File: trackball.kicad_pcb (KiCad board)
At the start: 6 copper layers, 65 x 85 mm, 241 parts, among them J2 ZX-PM2.0-2-4PY, Q1 XR2302, Q2 XR2302, SW1 HX TC-5608-Y, SW2 HX TC-5608-Y, SW3 HX TC-5608-Y, SW4 HX TC-5608-Y, SW5 HX TC-5608-Y, SW6 HX TC-5608-Y, SW7 HX TC-5608-Y, SW8 HX TC-5608-Y, SW9 TS-1010-C-A, U1 USB-TYPE-C-017, U10 WS2812B, U11 WS2812B, U12 WS2812B, U13 WS2812B, U14 WS2812B, U15 WS2812B, U16 WS2812B, U17 WS2812B, U18 WS2812B, U19 WS2812B, U2 SY80004DQD, U20 WS2812B, U21 WS2812B, U3 SY80004DQD, U4 PMW3610, U5 PMW3610, U6 WS2812B, U7 WS2812B, U8 WS2812B, U9 WS2812B, X1 XL7EL89CKI-111YLC-32M

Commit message: feat: 1k dongle, rev5 hw (wip)
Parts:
- removed C16, C31: 0201B103K160NT, easyeda2kicad:C0201
- removed R35: RC-01W103JT, easyeda2kicad:R0201
- removed R36: 0201WMF1603TEE, easyeda2kicad:R0201
- removed U_RE1, U_RE2: GT-EVA01AA-L1, easyeda2kicad:RES-ADJ-SMD_GT-EVA01AA-L1
- added C61: GRM155R60J226ME11D, easyeda2kicad:C0402, F.Cu at (39.9, 40.6)
- added C64: GRM155R60J226ME11D, easyeda2kicad:C0402, F.Cu at (47.5, 47.2)
- added ENC1: EC05E1220401, easyeda2kicad:SW-SMD_EC05E1220401, F.Cu at (67.5, 67.1)
- added ENC2: EC05E1220401, easyeda2kicad:SW-SMD_EC05E1220401, F.Cu at (67.5, 78.1)
- added Q3: AO3415A_C5350990, easyeda2kicad:SOT-23-3_L2.9-W1.6-P1.90-LS2.8-BR, F.Cu at (42.7, 42.2)
- added Q4: XR2302, easyeda2kicad:SOT-23-3_L2.9-W1.3-P0.95-LS2.4-BR, F.Cu at (46.1, 42.4)
- added R23: 0201WMF1603TEE, easyeda2kicad:R0201, F.Cu at (48.7, 44.9)
- added R49: RC-01W103JT, easyeda2kicad:R0201, F.Cu at (48.4, 43.9)
- added R6: RC-01W103JT, easyeda2kicad:R0201, F.Cu at (76.6, 47.7)
- added R7: RC-01W103JT, easyeda2kicad:R0201, F.Cu at (43.8, 44.1)
- added R8: RC-01W103JT, easyeda2kicad:R0201, F.Cu at (44.9, 40.7)
- added U22: TPS2116DRLR, easyeda2kicad:SOT-583-8_L2.1-W1.6-P0.50-LS1.6-BL, F.Cu at (45.6, 45.6)
- C30: value 0201B103K160NT -> 0201B821K500NT
- J2: value ZX-PM2.0-2-4PY -> AFH34-S08FIA-1H; footprint easyeda2kicad:HDR-TH_8P-P2.00-V-F-R2-C4-S2.00 -> easyeda2kicad:FPC-SMD_8P-P0.50_JS_AFH34-S08FIA-1H
- R12, R13, R14, R21: value RC-01W103JT -> RC0201JR-075K1L
- R18: value RT0402BRE0750RL -> RC-01W103JT; footprint easyeda2kicad:R0402 -> easyeda2kicad:R0201
- R22: value 0201WMF1603TEE -> RC0201JR-075K1L
- R3, R50, R51: value ~ -> (none)
- SW9: value TS-1010-C-A -> (none)
- moved R22 39.8 mm to (58.3, 43.7)
- moved R21 37.3 mm to (71.2, 45.3), turned to -90 degrees
- moved R32 10.4 mm to (38.7, 66.4)
- moved Q2 8.53 mm to (51.4, 45.3)
- moved R27 5.13 mm to (71.2, 117.1)
- moved R31 4.93 mm to (36.9, 93.9), turned to 90 degrees
- moved C66 2.78 mm to (50.0, 40.7), turned to -90 degrees
- moved R18 2.75 mm to (47.4, 45.2), turned to -90 degrees
- moved C32 2.02 mm to (71.5, 118.0), turned to 180 degrees
- moved R9 1.98 mm to (48.4, 40.9), turned to 0 degrees
- moved R34 1.44 mm to (70.8, 119.1), turned to 0 degrees
- moved J2 1.43 mm to (91.0, 115.1), turned to -135 degrees
- moved R28 1.17 mm to (89.5, 60.2)
- moved R12 1.09 mm to (41.0, 46.6), turned to 90 degrees
- moved R13 1.09 mm to (42.0, 46.2), turned to -90 degrees
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- renumbered ENC.ANY to ENC.ANY.1, ENC.ANY to ENC.ANY.2, SENS.ANY to SENS.ANY.1, SENS.ANY to SENS.ANY.2
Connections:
- C10 pad 1: BAT_VCC -> Net-(Q3-D)
- C15 pad 1: VSYS -> VLOAD
- C18 pad 1: VSYS -> VLOAD
- C3 pad 1: VSYS -> VLOAD
- C5 pad 1: VSYS -> VLOAD
- C7 pad 1: BAT_VCC -> Net-(Q3-D)
- D2 pad 1: SW2 -> SW2_WK
- D2 pad 2: SW1 -> SW1_WK
- D3 pad 1: SW4 -> SW4_WK
- D3 pad 2: SW3 -> SW3_WK
- D4 pad 1: SW6 -> SW6_WK
- D4 pad 2: SW5 -> SW5_WK
- D5 pad 1: SW8 -> SW8_WK
- D5 pad 2: SW7 -> SW7_WK
- ENC.ANY.1 pad 1: D_RE2_1V8 -> D_RE1_1V8
- ENC.ANY.1 pad 2: D_RE2_SW -> D_RE1_GND
- ENC.ANY.1 pad 3: D_RE2_A -> D_RE1_A
- ENC.ANY.1 pad 4: D_RE2_GND -> D_RE1_GND
- ENC.ANY.1 pad 5: D_RE2_B -> D_RE1_B
- ENC.ANY.1 pad 6: D_RE2_GND -> D_RE1_GND
- ENC.ANY.1 pad 7: D_RE2_GND -> D_RE1_GND
- ENC.ANY.1 pad 8: D_RE2_GND -> D_RE1_GND
- ENC.ANY.2 pad 1: D_RE1_1V8 -> D_RE2_1V8
- ENC.ANY.2 pad 2: D_RE1_SW -> D_RE2_GND
- ENC.ANY.2 pad 3: D_RE1_A -> D_RE2_A
- ENC.ANY.2 pad 4: D_RE1_GND -> D_RE2_GND
- ENC.ANY.2 pad 5: D_RE1_B -> D_RE2_B
- ENC.ANY.2 pad 6: D_RE1_GND -> D_RE2_GND
- ENC.ANY.2 pad 7: D_RE1_GND -> D_RE2_GND
- ENC.ANY.2 pad 8: D_RE1_GND -> D_RE2_GND
- ENC.L pad 7: RE1_SW -> GND
- ENC.R pad 7: RE2_SW -> GND
- J2 pad 1: MCU_SWDCLK -> GND
- J2 pad 2: 1V8 -> MCU_SWDCLK
- J2 pad 3: 3V3_EN -> 1V8
- J2 pad 4: 3V3 -> MCU_SWDIO
- J2 pad 5: MCU_SWDIO -> GND
- J2 pad 6: MCU_RESET -> GND
- J2 pad 7: GND -> 1V8
- J2 pad 8: USB_VBUS -> MCU_RESET
- R12 pad 1: 1V8 -> CHG_SDA
- R12 pad 2: CHG_SCL -> 1V8
- R13 pad 1: CHG_SDA -> 1V8
- R13 pad 2: 1V8 -> CHG_SCL
- R14 pad 1: CHG_IRQ -> 1V8
- R14 pad 2: 1V8 -> CHG_IRQ
- R15 pad 2: VSYS -> VLOAD
- R16 pad 1: Net-(R16-Pad1) -> SW8_WK
- R17 pad 1: Net-(R17-Pad1) -> SW7_WK
- R18 pad 1: GND -> Net-(U22-PR1)
- R18 pad 2: MCU_VIB_EN -> USB_VBUS
- R19 pad 1: Net-(R19-Pad1) -> SW1_WK
- R20 pad 1: Net-(R20-Pad1) -> SW2_WK
- R21 pad 1: D_RE1_SW -> Net-(U1-CC1)
- R21 pad 2: Net-(R21-Pad2) -> GND
- R22 pad 1: D_RE1_1V8 -> Net-(U1-CC2)
- R22 pad 2: Net-(R21-Pad2) -> GND
- R26 pad 1: Net-(R26-Pad1) -> SW5_WK
- R27 pad 1: Net-(R27-Pad1) -> SW6_WK
- R29 pad 1: Net-(R29-Pad1) -> SW4_WK
- R30 pad 1: Net-(R30-Pad1) -> SW3_WK
- R31 pad 1: Net-(R29-Pad1) -> SW4_WK
- R32 pad 1: Net-(R30-Pad1) -> SW3_WK
- R33 pad 1: Net-(R26-Pad1) -> SW5_WK
- R34 pad 1: Net-(R27-Pad1) -> SW6_WK
- R37 pad 1: Net-(R19-Pad1) -> SW1_WK
- R38 pad 1: Net-(R20-Pad1) -> SW2_WK
- R39 pad 1: Net-(R16-Pad1) -> SW8_WK
- R4 pad 1: BAT_VCC -> Net-(Q3-D)
- R40 pad 1: Net-(R17-Pad1) -> SW7_WK
- R54 pad 2: VSYS -> VLOAD
- R65 pad 2: VSYS -> VLOAD
- SENS.L pad 9: unconnected-(SENS.L1-Pad9) -> USB_VBUS
- SW1 pad 1: Net-(R19-Pad1) -> SW1_WK
- SW2 pad 1: Net-(R20-Pad1) -> SW2_WK
- SW3 pad 1: Net-(R30-Pad1) -> SW3_WK
- SW4 pad 1: Net-(R29-Pad1) -> SW4_WK
- SW5 pad 1: Net-(R26-Pad1) -> SW5_WK
- SW6 pad 1: Net-(R27-Pad1) -> SW6_WK
- SW7 pad 1: Net-(R17-Pad1) -> SW7_WK
- SW8 pad 1: Net-(R16-Pad1) -> SW8_WK
- SW9 pad 3: unconnected-(SW9-Pad3) -> GND
- SW9 pad 4: unconnected-(SW9-Pad4) -> GND
- U1 pad A5: USB_CC1 -> Net-(U1-CC1)
- U1 pad B5: USB_CC2 -> Net-(U1-CC2)
- U2 pad 6: VSYS -> VLOAD
- U3 pad 6: VSYS -> VLOAD
- U_CHG1 pad 26: USB_CC1 -> unconnected-(U_CHG1-CC1-Pad26)
- U_CHG1 pad 27: USB_CC2 -> unconnected-(U_CHG1-CC2-Pad27)
- U_CHG1 pad 7: BAT_VCC -> Net-(Q3-D)
- U_MCU1 pad AD10: RE1_SW -> ARB2
- U_MCU1 pad T2: RE2_SW -> ARB1
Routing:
- net VLOAD: track 0.00 -> 96.0 mm, vias 0 -> 5
- net VSYS: track 97.6 -> 13.7 mm, vias 5 -> 0
- net 3V3_EN: track 179.6 -> 118.2 mm
- net USB_VBUS: track 183.7 -> 137.5 mm
- net 3V3: track 242.0 -> 203.8 mm, vias 16 -> 14
- net 1V8: track 308.7 -> 270.6 mm, vias 30 -> 28
- net RE1_SW: track 37.6 -> 0.00 mm, vias 2 -> 0
- net RE2_SW: track 35.3 -> 0.00 mm, vias 2 -> 0
- net Net-(Q3-D): track 0.00 -> 33.3 mm, vias 0 -> 4
- net USB_CC1: track 25.7 -> 0.00 mm, vias 2 -> 0
- net SW1_WK: track 0.00 -> 24.2 mm
- net USB_CC2: track 24.2 -> 0.00 mm
- net SW7_WK: track 0.00 -> 22.7 mm, vias 0 -> 2
- net SW4_WK: track 0.00 -> 20.9 mm
- net D_RE2_GND: track 7.84 -> 28.5 mm, vias 5 -> 3
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- added copper zone on B.Cu, net D_RE1_GND
- added copper zone on F.Cu, net D_RE1_GND
- added copper zone on In2.Cu, net D_RE1_GND
- added copper zone on In3.Cu, net D_RE1_GND
- added copper zone on B.Cu, net D_RE2_GND
- added copper zone on F.Cu, net D_RE2_GND
- added copper zone on In2.Cu, net D_RE2_GND
- added copper zone on In3.Cu, net D_RE2_GND
- removed copper zone on In2.Cu, net D_RE1_1V8
- removed copper zone on In3.Cu, net D_RE1_1V8
- removed copper zone on In2.Cu, net D_RE2_1V8
- removed copper zone on In3.Cu, net D_RE2_1V8
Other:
- board text added: "21/01/26"
- board text added: "Jan 2026"
- board text added: "RST"
- board text added: "rev. 05"
- board text removed: "16/10/25"
- board text removed: "Oct 2025"
- board text removed: "rev. 04"

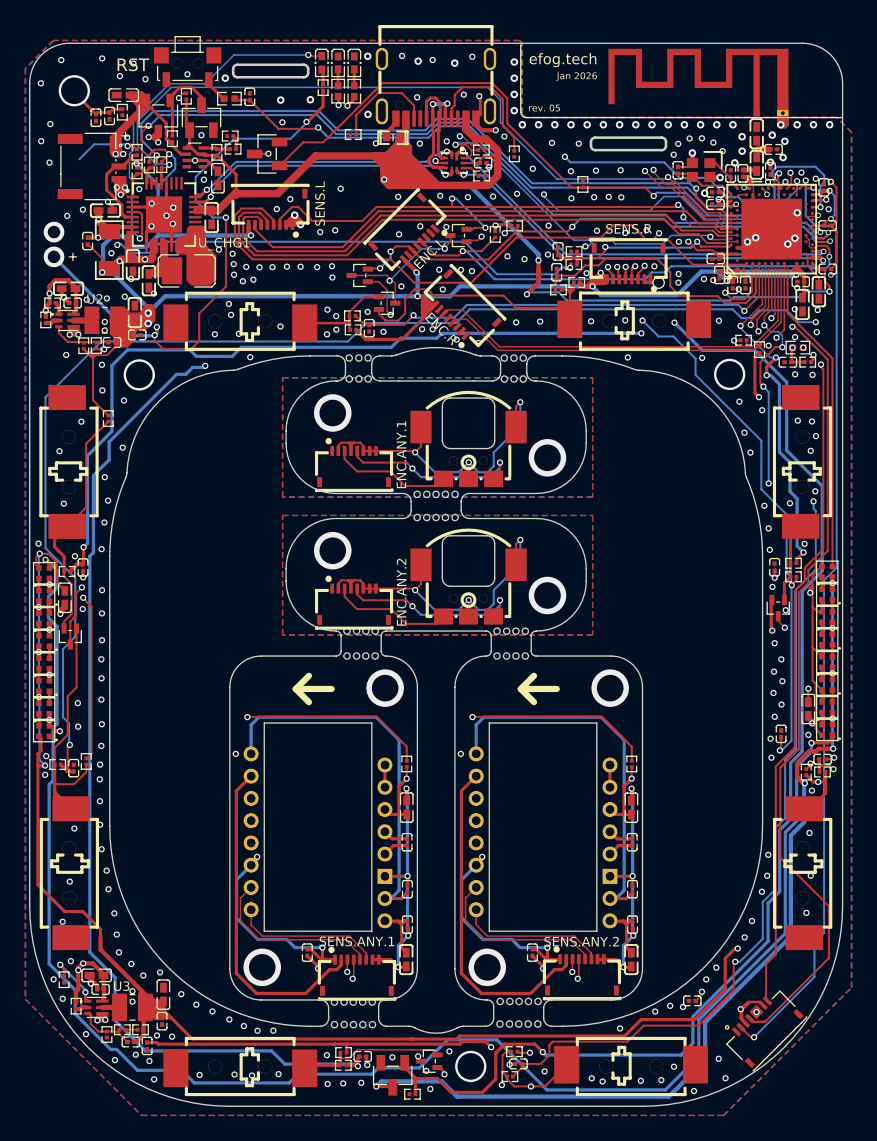
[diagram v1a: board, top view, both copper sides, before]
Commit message: chore: rev5 hw fixes
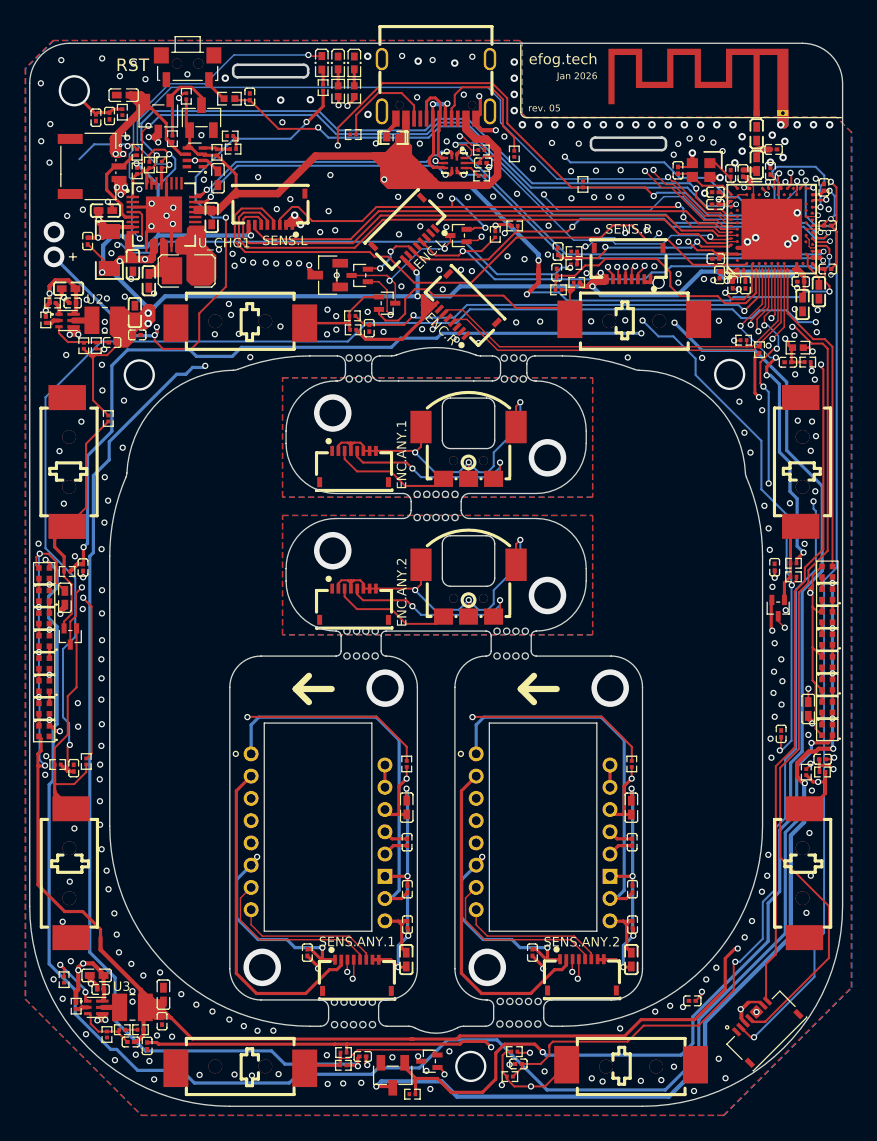
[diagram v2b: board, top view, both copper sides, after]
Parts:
- moved Q2 10.8 mm to (56.2, 55.0)
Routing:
- net VIB_GND: track 25.0 -> 35.3 mm
- net MCU_VIB_EN: track 59.5 -> 67.0 mm, vias 2 -> 4
- net Net-(D2-Pad3): track 181.8 -> 183.2 mm
- net SW6: track 87.6 -> 86.9 mm
- net SS1_CLK: track 45.3 -> 44.8 mm
- net RGB_DOUT: track 25.2 -> 25.8 mm
- net SS1_DIO: track 41.3 -> 40.8 mm
- net MCU_SWDIO: track 76.3 -> 76.8 mm
- net SS1_NCS: track 47.2 -> 46.7 mm
- net GND: vias 329 -> 326
